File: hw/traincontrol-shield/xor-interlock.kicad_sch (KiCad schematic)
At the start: 4 parts, among them U3 74LVC1G86, U4 74LVC2G08

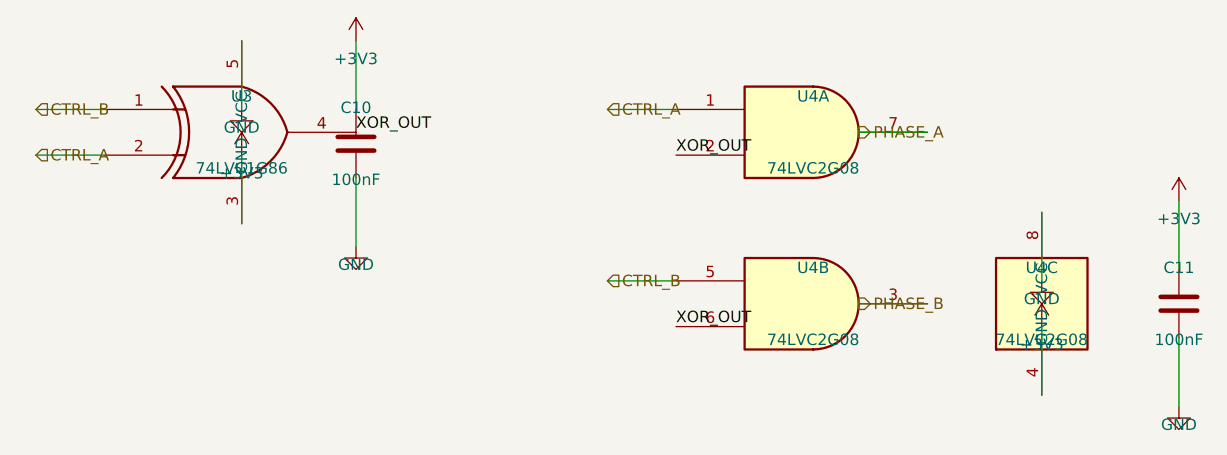
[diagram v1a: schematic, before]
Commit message: Fix hierarchical label orientations: angle=0 → angle=180 throughout
All hlabel calls in zero-crossing, xor-interlock, opto-triac-drive, and
rail-voltage-sense sub-sheets were using angle=0, causing the label arrows
to point in the wrong direction. Changed to angle=180 uniformly; for
left-side labels also shifted x by −STUB so the label connection pin
coincides with the circuit element, keeping the label body outside the
schematic area.

Co-Authored-By: Claude Sonnet 4.6 <noreply@anthropic.com>
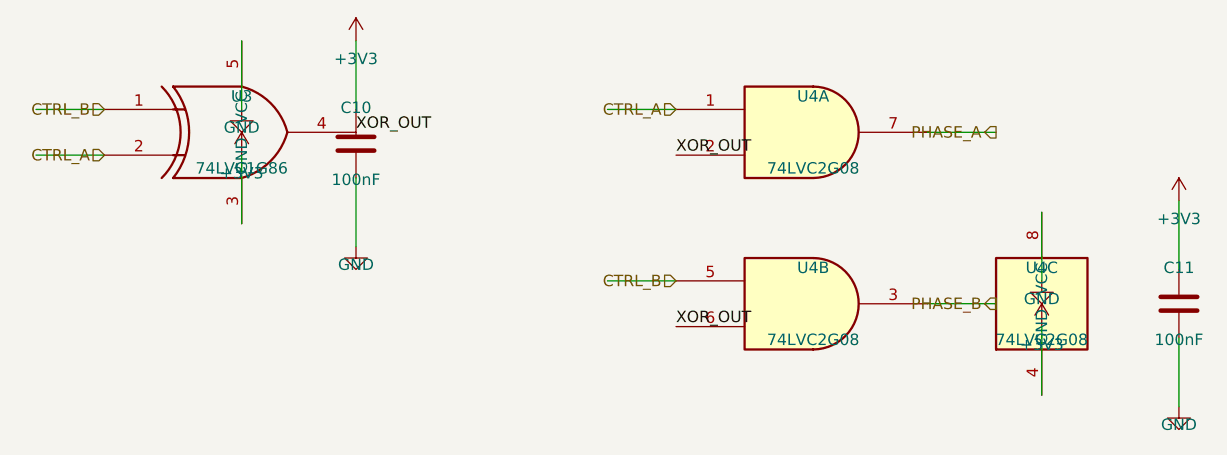
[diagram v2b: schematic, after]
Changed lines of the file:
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@@
 	(hierarchical_label "CTRL_A"
 		(shape input)
-		(at 40.64 92.71 0)
+		(at 48.26 92.71 180)
 		(fields_autoplaced yes)
-		(effects (font (size 1.27 1.27)) (justify left bottom))
+		(effects (font (size 1.27 1.27)) (justify right bottom))
 		(property "Intersheetrefs" "${INTERSHEET_REFS}"
-			(at 40.64 92.71 0)
+			(at 48.26 92.71 0)
 			(effects (font (size 1.27 1.27)) (hide yes))
 		)
@@
 	(hierarchical_label "CTRL_B"
 		(shape input)
-		(at 40.64 87.63 0)
+		(at 48.26 87.63 180)
 		(fields_autoplaced yes)
-		(effects (font (size 1.27 1.27)) (justify left bottom))
+		(effects (font (size 1.27 1.27)) (justify right bottom))
 		(property "Intersheetrefs" "${INTERSHEET_REFS}"
-			(at 40.64 87.63 0)
+			(at 48.26 87.63 0)
 			(effects (font (size 1.27 1.27)) (hide yes))
 		)
@@
 	(hierarchical_label "CTRL_A"
 		(shape input)
-		(at 104.14 87.63 0)
+		(at 111.76 87.63 180)
 		(fields_autoplaced yes)
-		(effects (font (size 1.27 1.27)) (justify left bottom))
+		(effects (font (size 1.27 1.27)) (justify right bottom))
 		(property "Intersheetrefs" "${INTERSHEET_REFS}"
-			(at 104.14 87.63 0)
+			(at 111.76 87.63 0)
 			(effects (font (size 1.27 1.27)) (hide yes))
 		)
@@
 	(hierarchical_label "CTRL_B"
 		(shape input)
-		(at 104.14 106.68 0)
+		(at 111.76 106.68 180)
 		(fields_autoplaced yes)
-		(effects (font (size 1.27 1.27)) (justify left bottom))
+		(effects (font (size 1.27 1.27)) (justify right bottom))
 		(property "Intersheetrefs" "${INTERSHEET_REFS}"
-			(at 104.14 106.68 0)
+			(at 111.76 106.68 0)
 			(effects (font (size 1.27 1.27)) (hide yes))
 		)
 	)
 	(wire
-		(pts (xy 132.07999999999998 90.17) (xy 139.7 90.17))
+		(pts (xy 139.7 90.17) (xy 147.32 90.17))
 		(stroke (width 0) (type solid))
 	)
 	(hierarchical_label "PHASE_A"
 		(shape output)
-		(at 132.07999999999998 90.17 0)
+		(at 147.32 90.17 180)
 		(fields_autoplaced yes)
-		(effects (font (size 1.27 1.27)) (justify left bottom))
+		(effects (font (size 1.27 1.27)) (justify right bottom))
 		(property "Intersheetrefs" "${INTERSHEET_REFS}"
-			(at 132.07999999999998 90.17 0)
+			(at 147.32 90.17 0)
 			(effects (font (size 1.27 1.27)) (hide yes))
 		)
 	)
 	(wire
-		(pts (xy 132.07999999999998 109.22) (xy 139.7 109.22))
+		(pts (xy 139.7 109.22) (xy 147.32 109.22))
 		(stroke (width 0) (type solid))
 	)
 	(hierarchical_label "PHASE_B"
 		(shape output)
-		(at 132.07999999999998 109.22 0)
+		(at 147.32 109.22 180)
 		(fields_autoplaced yes)
-		(effects (font (size 1.27 1.27)) (justify left bottom))
+		(effects (font (size 1.27 1.27)) (justify right bottom))
 		(property "Intersheetrefs" "${INTERSHEET_REFS}"
-			(at 132.07999999999998 109.22 0)
+			(at 147.32 109.22 0)
 			(effects (font (size 1.27 1.27)) (hide yes))
 		)
